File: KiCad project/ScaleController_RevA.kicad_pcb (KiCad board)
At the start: 4 copper layers, 89.9 x 52.8 mm, 60 parts, among them J1 USB_C_Receptacle_USB2.0_16P, J3 MTMM-103-03-T-S-150, J5 MTMM-103-03-T-S-150, J6 Conn_01x05, J7 MTMM-103-03-T-S-150, J8 MTMM-103-03-T-S-150, J9 Conn_01x04_Socket, Q2 BC817, Q3 BC817, SW1 1101NE, SW2 1101NE, U2 LM1117MPX-3.3_NOPB, U3 ESP32-C3-WROOM-02-H4, U4 CP2102N-A02-GQFN20, U5 USBLC6-2SC6, U6 HX711

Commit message: Pre-order tidy: DRU, symbol-lib sync, PCBWay stackup, JST part number on J3/5/7/8
- .kicad_dru: drop the global annular_width ignore. U3's ground-grid pads
  are 0.6/0.3 mm since the DFM pass; DRC is identical without the rule.
- Project symbol libs for LM1117MPX-3.3_NOPB, ESP32-C3-WROOM-02-H4 and
  MTMM-103-03-T-S-150 rewritten in KiCad 9 format from the schematic
  copies (the MTMM copy has pins 1/2/3 to match the JST PH pads; the old
  lib still had 01/02/03). SnapEDA "Description_1" junk fields removed
  from libs, embedded copies and instances. ERC: 0 lib_symbol_mismatch.
- Stackup: PCBWay standard 4-layer 1.6 mm (7628 prepreg 0.19 x2,
  core 1.03, 1 oz all layers).
- J3/J5/J7/J8: Value/MF/MP -> JST B3B-PH-K-S in schematic, project lib
  and board footprints; stale Samtec/SnapEDA fields dropped. Symbol name
  and lib_id left as MTMM-103-03-T-S-150.

Netlist nets/pins identical before and after. DRC with schematic parity:
0 errors, 0 unconnected, 0 parity issues, 5 known benign warnings.

Co-Authored-By: Claude Fable 5.1 <noreply@anthropic.com>
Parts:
- J3, J5, J7, J8: value MTMM-103-03-T-S-150 -> B3B-PH-K-S

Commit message: BOM fixes, DRC exclusions, edge-clearance restore, fab outputs and order notes
- C9 value 4.7u -> 10u (matches its KEMET T491A 10 uF part number; LM1117
  output cap). Capacitor values normalised to 0.1u / 1u / 10u so identical
  0805 parts group: BOM 30 -> 27 lines.
- J1 value -> HRO TYPE-C-31-M-12, MF/MP fields added (schematic + board).
- min_copper_edge_clearance restored to 0.3 mm. The DFM commit 4617449 set
  it; the GUI refill save in 61ca090 wrote the old project file back (0.2).
  Board meets 0.3 (probe rule: no violations).
- DRC exclusions for the 4 silk-over-edge warnings (J1 face, U3 antenna
  notch), added in the GUI.
- docs/pcbway-order-notes.md: board spec, stackup, drills, special notes.
- docs/status-2026-09-18.md: supersedes 17 Sept; kicad-cli regen commands.
- TODO: fabrication items ticked.

Fab package generated to fabrication/RevA-2026-09-18/ (git-ignored):
schematic PDF, BOM (raw + PCBWay), Gerbers/drill zip, pos top/bottom.
Netlist nets/pins identical to bdae270. DRC + parity: 0 errors,
0 unconnected, 0 parity; 4 excluded + 1 intentional warning.

Co-Authored-By: Claude Fable 5.1 <noreply@anthropic.com>
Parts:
- C14: value 1 µF -> 1u
- C15, C17: value 0.1 µF -> 0.1u
- C16: value 10 µF -> 10u
- C9: value 4.7u -> 10u
- J1: value USB_C_Receptacle_USB2.0_16P -> TYPE-C-31-M-12
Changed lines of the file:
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@@
 			)
 		)
-		(property "Value" "4.7u"
+		(property "Value" "10u"
 			(at 0 0 90)
 			(layer "F.SilkS")
@@
 			)
 		)
-		(property "Value" "1 µF"
+		(property "Value" "1u"
 			(at 0 1.68 0)
 			(layer "F.Fab")
@@
 			)
 		)
-		(property "Value" "USB_C_Receptacle_USB2.0_16P"
+		(property "Value" "TYPE-C-31-M-12"
 			(at 0 5.1 0)
 			(layer "F.Fab")
@@
 			)
 		)
+		(property "MF" "HRO"
+			(at 0 0 0)
+			(unlocked yes)
+			(layer "F.Fab")
+			(hide yes)
+			(effects
+				(font
+					(size 1.27 1.27)
+					(thickness 0.15)
+				)
+			)
+		)
+		(property "MP" "TYPE-C-31-M-12"
+			(at 0 0 0)
+			(unlocked yes)
+			(layer "F.Fab")
+			(hide yes)
+			(effects
+				(font
+					(size 1.27 1.27)
+					(thickness 0.15)
+				)
+			)
+		)
 		(property "Description" "USB 2.0-only 16P Type-C Receptacle connector"
 			(at 0 0 0)
@@
 			)
 		)
-		(property "Value" "10 µF"
+		(property "Value" "10u"
 			(at 0 1.68 0)
 			(layer "F.Fab")
@@
 			)
 		)
-		(property "Value" "0.1 µF"
+		(property "Value" "0.1u"
 			(at 0 1.68 0)
 			(layer "F.Fab")
@@
 			)
 		)
-		(property "Value" "0.1 µF"
+		(property "Value" "0.1u"
 			(at 0 1.68 180)
 			(layer "F.Fab")

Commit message: Specify dielectric and source for the HX711 front-end parts in the BOM
- C12/C13: Value "4.7nF C0G 50V", description marks them as the matched
  HX711 input-filter pair, no Class 2 substitution.
- C16: Value "10u X7R 10V", description forbids Y5V.
- U6: MF/MP Avia Semiconductor HX711 added; description notes it is
  noise-critical and must be genuine or a known-good source.
- Order notes and status note updated accordingly.

Value fields are on F.Fab only; Gerbers unchanged. Netlist nets/pins
identical. DRC + parity: 0 errors, 0 parity issues.

Co-Authored-By: Claude Fable 5.1 <noreply@anthropic.com>
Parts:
- C12, C13: value 4.7nF -> 4.7nF C0G 50V
- C16: value 10u -> 10u X7R 10V
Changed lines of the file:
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@@
 			)
 		)
-		(property "Description" "24-bit Analog-to-Digital Converter (ADC) for Weight Scales, SOIC-16 (SOP-16)"
+		(property "MF" "Avia Semiconductor"
+			(at 0 0 0)
+			(unlocked yes)
+			(layer "F.Fab")
+			(hide yes)
+			(effects
+				(font
+					(size 1.27 1.27)
+					(thickness 0.15)
+				)
+			)
+		)
+		(property "MP" "HX711"
+			(at 0 0 0)
+			(unlocked yes)
+			(layer "F.Fab")
+			(hide yes)
+			(effects
+				(font
+					(size 1.27 1.27)
+					(thickness 0.15)
+				)
+			)
+		)
+		(property "Description" "24-bit ADC for weight scales, SOIC-16 - Avia Semiconductor HX711, genuine or known-good source (noise-critical)"
 			(at 0 0 0)
 			(layer "F.Fab")
@@
 			)
 		)
-		(property "Value" "4.7nF"
+		(property "Value" "4.7nF C0G 50V"
 			(at 0 1.68 0)
 			(layer "F.Fab")
@@
 			)
 		)
-		(property "Description" "Unpolarized capacitor"
+		(property "Description" "4.7 nF C0G/NP0 50 V, 0805 - HX711 input filter, matched pair with C13; do not substitute Class 2 dielectric"
 			(at 0 0 0)
 			(layer "F.Fab")
@@
 			)
 		)
-		(property "Value" "10u"
+		(property "Value" "10u X7R 10V"
 			(at 0 1.68 0)
 			(layer "F.Fab")
@@
 			)
 		)
-		(property "Description" "Unpolarized capacitor"
+		(property "Description" "10 uF X7R or X5R, 10 V min, 0805 - HX711 AVDD/DVDD decoupling; no Y5V"
 			(at 0 0 0)
 			(layer "F.Fab")
@@
 			)
 		)
-		(property "Value" "4.7nF"
+		(property "Value" "4.7nF C0G 50V"
 			(at 0 1.68 180)
 			(layer "F.Fab")
@@
 			)
 		)
-		(property "Description" "Unpolarized capacitor"
+		(property "Description" "4.7 nF C0G/NP0 50 V, 0805 - HX711 input filter, matched pair with C12; do not substitute Class 2 dielectric"
 			(at 0 0 180)
 			(layer "F.Fab")

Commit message: Board: native USB routing, strapping/I2C pull-ups, status LED; CP2102N section removed
Follows the schematic change (89ba36d) and the GUI "Update PCB from
Schematic" step. All copper edits made headlessly:
- Removed the 49 segments / 6 vias left on no net by the CP2102N section
  and the dangling GND/3.3V/BOOT/VBUS stubs around it.
- The five long B.Cu bus lines between the module and J6 are kept and
  re-terminated: top two now carry USB D+/D- from U5 (new F.Cu risers at
  x=142/143.5), the next two carry U0TXD/U0RXD from J6.3/J6.4, the fifth
  carries GPIO10 from J6.2 and is extended to module pad 10.
- GPIO8 and STATUS_LED leave the module to the right and run down the
  free B.Cu channel between the PD_SCK and SDA diagonals to a cluster
  (R3, R14, D5) between the module and the HX711.
- R4 (IO2), R7 (SCL), R6 (SDA) along the right edge strip; R5 (BOOT)
  next to the BOOT trace by LC1. All 3.3V ends via to the In2 plane.
- Silk: TX/RX removed, STATUS added, J6 labels IO10/TXD/RXD; R4/R6/R7
  reference silk hidden (would hang over the board edge).

DRC on a fill-stripped copy: 0 errors, 0 signal-net unconnected items;
zones need a refill in the GUI before the real DRC and the Gerber export.

Co-Authored-By: Claude Fable 5.1 <noreply@anthropic.com>
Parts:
- removed C10: 0.1u, Capacitor_SMD:C_0805_2012Metric
- removed C11: 1u, Capacitor_SMD:C_0805_2012Metric
- removed C9: 10u, Footprints:T491A
- removed D6: Red, Footprints:LEDC2012X120N
- removed Q2, Q3: BC817, Package_TO_SOT_SMD:SOT-23
- removed R11: 1K, Resistor_SMD:R_0805_2012Metric
- removed R12: 22K1, Resistor_SMD:R_0805_2012Metric
- removed R13: 47K5, Resistor_SMD:R_0805_2012Metric
- removed R18: 330, Resistor_SMD:R_0805_2012Metric
- removed R33, R34: 10K, Resistor_SMD:R_0805_2012Metric
- removed U4: CP2102N-A02-GQFN20, Package_DFN_QFN:SiliconLabs_QFN-20-1EP_3x3mm_P0.5mm_EP1.8x1.8mm
- added R3: 10K, Resistor_SMD:R_0805_2012Metric, F.Cu at (187.4, 99.3)
- added R4: 10K, Resistor_SMD:R_0805_2012Metric, F.Cu at (199.8, 81.5)
- added R5: 10K, Resistor_SMD:R_0805_2012Metric, F.Cu at (169.0, 99.5)
- added R6: 4K7, Resistor_SMD:R_0805_2012Metric, F.Cu at (199.3, 99.6)
- added R7: 4K7, Resistor_SMD:R_0805_2012Metric, F.Cu at (199.3, 96.0)
- moved D5 56.2 mm to (191.8, 99.3)
- moved R14 53.4 mm to (189.4, 99.3), turned to 270 degrees
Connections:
- J6 pad 2: /ESP32-C3-02/GPIO8 -> /ESP32-C3-02/GPIO10
- J6 pad 3: /ESP32-C3-02/GPIO18 -> /ESP32-C3-02/U0TXD
- J6 pad 4: /ESP32-C3-02/GPIO19 -> /ESP32-C3-02/U0RXD
- R14 pad 1: Net-(U4-~{TXT}/GPIO.2) -> /ESP32-C3-02/STATUS_LED
- U3 pad 10: unconnected-(U3-IO10-Pad10) -> /ESP32-C3-02/GPIO10
- U3 pad 11: /ESP32-C3-02/TX_RX -> /ESP32-C3-02/U0RXD
- U3 pad 12: /ESP32-C3-02/RX_TX -> /ESP32-C3-02/U0TXD
- U3 pad 13: /ESP32-C3-02/GPIO18 -> /ESP32-C3-02/USB_D-
- U3 pad 14: /ESP32-C3-02/GPIO19 -> /ESP32-C3-02/USB_D+
- U3 pad 16: unconnected-(U3-IO2-Pad16) -> /ESP32-C3-02/IO2
- U3 pad 6: unconnected-(U3-IO7-Pad6) -> /ESP32-C3-02/STATUS_LED
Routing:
- net /ESP32-C3-02/GPIO10: track 0.00 -> 107.4 mm, vias 0 -> 2
- net /ESP32-C3-02/U0RXD: track 0.00 -> 105.3 mm, vias 0 -> 2
- net /ESP32-C3-02/GPIO19: track 103.8 -> 0.00 mm, vias 2 -> 0
- net /ESP32-C3-02/U0TXD: track 0.00 -> 101.2 mm, vias 0 -> 1
- net /ESP32-C3-02/GPIO18: track 100.6 -> 0.00 mm, vias 1 -> 0
- net /ESP32-C3-02/RX_TX: track 85.0 -> 0.00 mm, vias 2 -> 0
- net /ESP32-C3-02/TX_RX: track 84.8 -> 0.00 mm, vias 2 -> 0
- net /ESP32-C3-02/USB_D+: track 6.06 -> 90.1 mm, vias 0 -> 2
- net /ESP32-C3-02/USB_D-: track 6.06 -> 87.7 mm, vias 0 -> 2
- net /ESP32-C3-02/GPIO8: track 92.3 -> 12.4 mm
- net /ESP32-C3-02/RTS: track 39.0 -> 0.00 mm
- net /ESP32-C3-02/DTS: track 25.3 -> 0.00 mm, vias 2 -> 0
- net Net-(Q2-B): track 23.6 -> 0.00 mm
- net Net-(Q3-B): track 16.7 -> 0.00 mm, vias 2 -> 0
- net /ESP32-C3-02/STATUS_LED: track 0.00 -> 15.5 mm, vias 0 -> 2
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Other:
- board text added: "IO10"
- board text added: "RXD"
- board text added: "STATUS"
- board text added: "TXD"
- board text removed: "IO18"
- board text removed: "IO19"
- board text removed: "IO8"
- board text removed: "RX"
- board text removed: "TX"

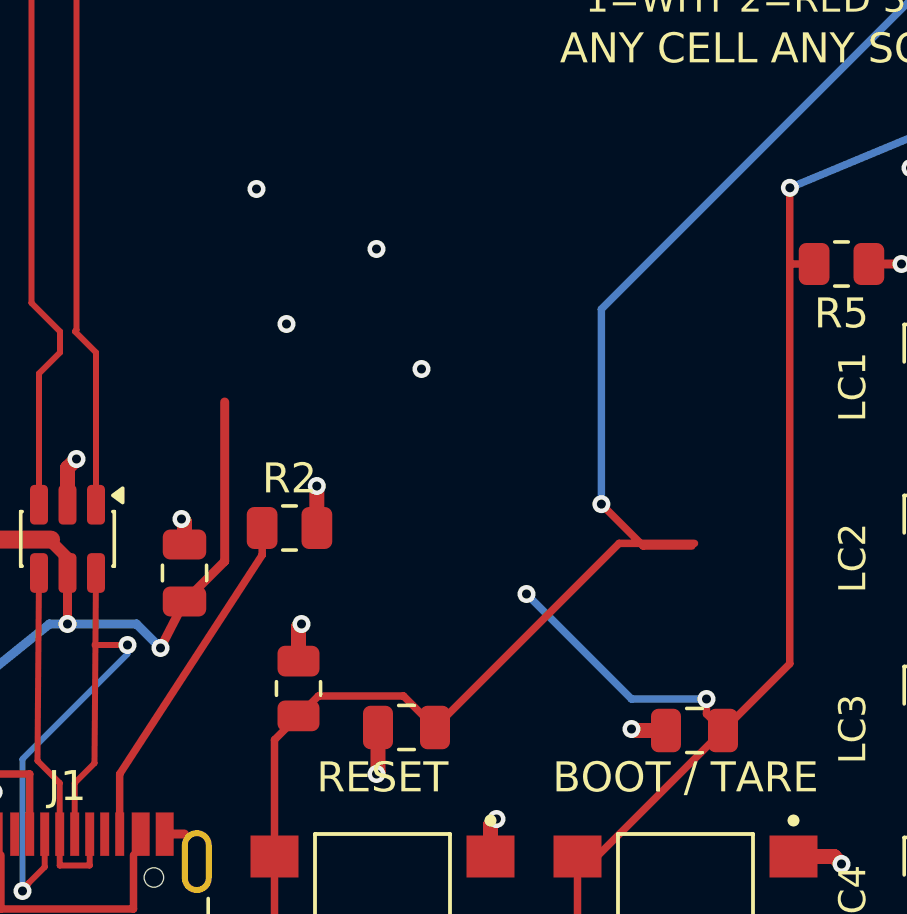
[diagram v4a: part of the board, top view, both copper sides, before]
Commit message: Board: zones refilled (GUI); remove the last dead copper from the CP2102N/Q3 removal; docs updated
- Removed 4 orphan plane vias, the dead BOOT branch that fed Q3 (2 vias,
  4 segments) and the VBUS stub that fed the removed sense divider.
- DRC on the refilled board: 0 errors, 0 unconnected, 0 parity issues;
  remaining warnings are the 4 excluded silk items and the intentional
  U3 library note.
- Order notes: 44 parts / 23 BOM lines, no 0.55 mm via, no via-in-pad,
  native USB note. Status note: rework section, regenerated package.
  TODO: review findings F1-F5 closed in Rev-A.

Co-Authored-By: Claude Fable 5.1 <noreply@anthropic.com>
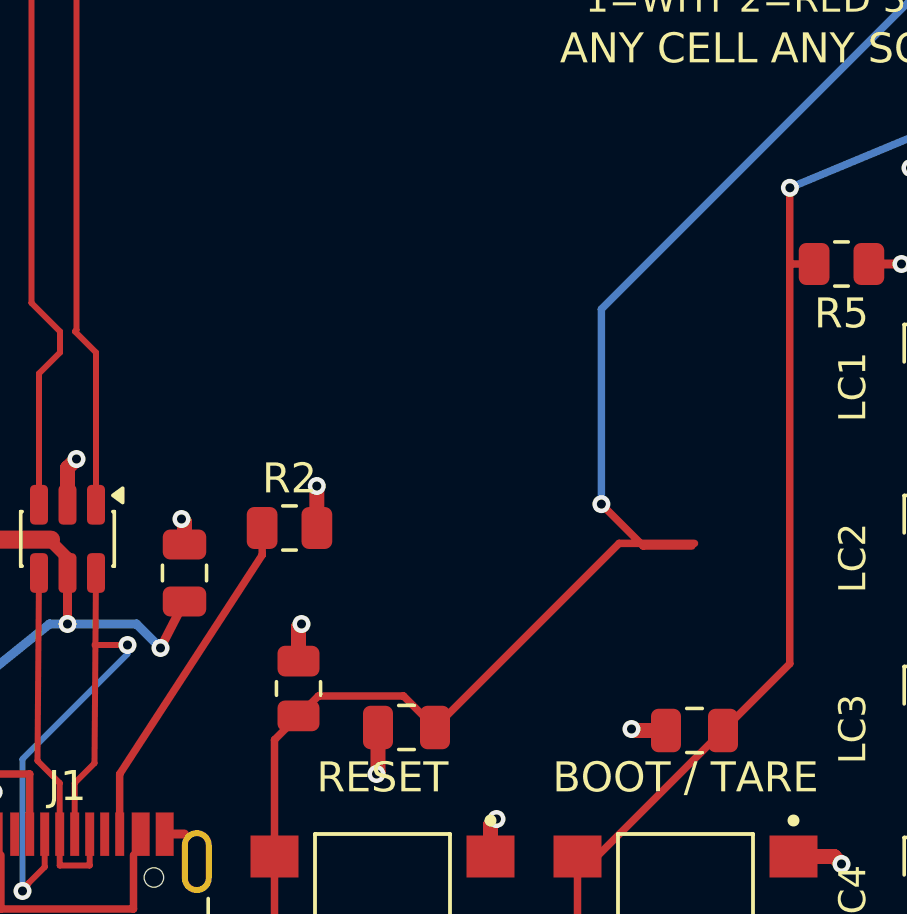
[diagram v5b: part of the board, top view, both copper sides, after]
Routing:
- net /ESP32-C3-02/BOOT: track 53.8 -> 45.1 mm, vias 4 -> 2
- net /VBUS: track 39.6 -> 32.4 mm
- net GND: vias 26 -> 23
- net 3.3V: vias 13 -> 12
